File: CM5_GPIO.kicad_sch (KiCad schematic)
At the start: 42 parts, among them J14 JST_BM04B-SRSS-TB, J16 JST_BM04B-SRSS-TB, J19 Conn_1x03_Male, J2 Conn_2x07_Male, J3 Conn_1x03_Male, J7 Micro_SD_Card_Det, J8 Conn_2x20_Male, SW1 Right angle Tact button, SW2 Right angle Tact button, U1 TPD4EUSB30, U16 SN74AHCT1G125DRLR, U17 TCA9538DBR, U18 RT9742GGJ5, U2 TPD4EUSB30, U3 MagJack-A70-112-331N126, U5 74LVC1G07SE-7, U9 SK6812

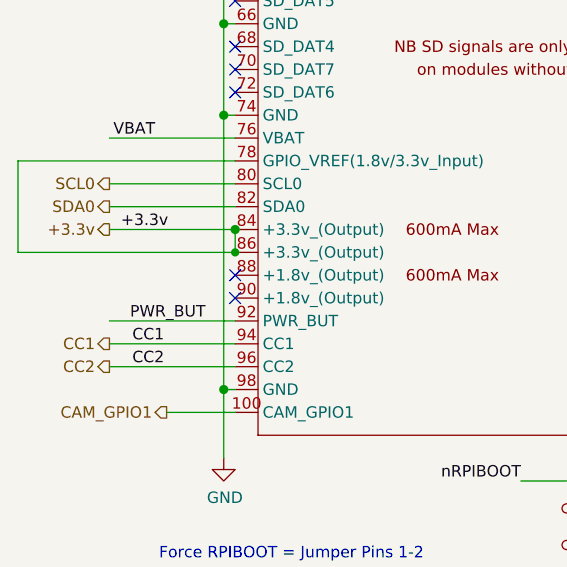
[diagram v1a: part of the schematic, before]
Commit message: USB hub: run the 24 MHz oscillator Y1 from the CM5 1.8 V output
Y1 (ECS-2520MV, 1.6-3.6 V supply) was powered from +3.3 V and drove
U11 XI (pin 30) with a 3.3 V clock. XI is rated 2.45 V absolute maximum
and TI requires a 1.8 V clock source (TUSB4041I datasheet 5.1, 6.3.6).

- Y1 VDD and its decoupling cap C50 move from +3.3v to a new +1V8 net.
- +1V8 comes from the CM5's +1.8 V output pins 88/90 (600 mA total),
  which were unused (no-connect flags removed).
- Y1 tri-state pin 1 gets a no-connect flag: open = output enabled per
  the ECS-2520MV datasheet.

Note: Y1's Value field says ECS-2520MV-240-CN-TR while its MPN/Digikey
fields say -DN-TR (C = +/-25 ppm, D = +/-20 ppm); both meet the hub's
+/-100 ppm. Left as is for the BOM owner to reconcile.

Refs #24 (verify on hardware before closing).

Co-Authored-By: Claude Opus 5.5 <noreply@anthropic.com>
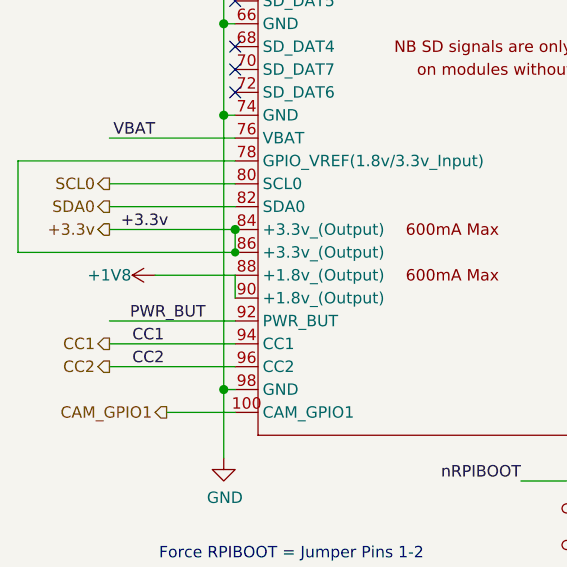
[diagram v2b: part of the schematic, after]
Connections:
- net +1V8: now reaches Module1.88 (+1.8v_(Output))
- net +1V8: now also Module1.90 (+1.8v_(Output))
- no-connect marks 13 -> 11
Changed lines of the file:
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@@
 	)
 	(no_connect
-		(at 39.37 130.81)
-	)
-	(no_connect
 		(at 39.37 107.95)
 	)
@@
 	)
 	(no_connect
-		(at 39.37 133.35)
-	)
-	(no_connect
 		(at 39.37 105.41)
 	)
@@
 	(wire
 		(pts
+			(xy 30.48 130.81) (xy 39.37 130.81)
+		)
+		(stroke
+			(width 0)
+			(type default)
+		)
+	)
+	(wire
+		(pts
 			(xy 149.86 44.45) (xy 152.4 44.45)
 		)
@@
 	(wire
 		(pts
+			(xy 39.37 130.81) (xy 39.37 133.35)
+		)
+		(stroke
+			(width 0)
+			(type default)
+		)
+	)
+	(wire
+		(pts
 			(xy 100.33 24.13) (xy 113.03 24.13)
 		)
@@
 					(unit 1)
 				)
+			)
+		)
+	)
+	(symbol
+		(lib_id "power:+1V8")
+		(at 30.48 130.81 90)
+		(unit 1)
+		(body_style 1)
+		(exclude_from_sim no)
+		(in_bom yes)
+		(on_board yes)
+		(in_pos_files yes)
+		(dnp no)
+		(property "Reference" "#PWR001"
+			(at 34.29 130.81 0)
+			(hide yes)
+			(show_name no)
+			(do_not_autoplace no)
+			(effects
+				(font
+					(size 1.27 1.27)
+				)
+			)
+		)
+		(property "Value" "+1V8"
+			(at 25.4 130.81 90)
+			(show_name no)
+			(do_not_autoplace no)
+			(effects
+				(font
+					(size 1.27 1.27)
+				)
+			)
+		)
+		(property "Footprint" ""
+			(at 30.48 130.81 0)
+			(hide yes)
+			(show_name no)
+			(do_not_autoplace no)
+			(effects
+				(font
+					(size 1.27 1.27)
+				)
+			)
+		)
+		(property "Datasheet" ""
+			(at 30.48 130.81 0)
+			(hide yes)
+			(show_name no)
+			(do_not_autoplace no)
+			(effects
+				(font
+					(size 1.27 1.27)
+				)
+			)
+		)
+		(property "Description" "Power symbol creates a global label with name \"+1V8\""
+			(at 30.48 130.81 0)
+			(hide yes)
+			(show_name no)
+			(do_not_autoplace no)
+			(effects
+				(font
+					(size 1.27 1.27)
+				)
+			)
+		)
+		(pin "1"
+		)
+		(instances
+			(project "libreboard"
+				(path "/e63e39d7-6ac0-4ffd-8aa3-1841a4541b55/00000000-0000-0000-0000-00005cff706a"
+					(reference "#PWR001")
+					(unit 1)
+				)

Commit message: USB hub: software-controlled hub reset from TCA9538 P7
The CM5 can now hard-reset the TUSB4041 hub over I2C, without
power-cycling anything else.

- U17 (TCA9538) P7 drives new net HUB_SW_RESETz into the manual-reset
  input (MR, pin 3) of the hub supervisor U19 (TPS3808G01). MR has an
  internal ~90k pull-up and the TCA9538 has no I/O pull-ups, so at
  power-up (P7 = input) the supervisor alone controls GRSTz as before.
- To reset: write 0 to P7 in the output register (0x01), then clear bit
  7 of the configuration register (0x03) so P7 drives low; after ~1 ms
  set the bit again. U19 holds GRSTz low while MR is low and for its
  20 ms timeout after release, so the hub always gets a valid (>= 3 ms)
  reset pulse regardless of software timing.
- U17 A0/A1 were floating; both now go to GND, fixing the expander at
  0x70 on i2c-0 (ID_SC/ID_SD), the address testscripts already use.
- Root sheet: HUB_SW_RESETz sheet pins on CM5_GPIO (out) and
  CM5_HighSpeed (in), wired like the other inter-sheet signals.

No new parts. PCB needs Update from Schematic and three short traces
(U17.12 to U19.3, U17.1 and U17.2 to GND). Netlist diff: only those
four pins change net. ERC 353 -> 348, only the U17 A0/A1/P7
unconnected warnings go away.

Refs #25.

Co-Authored-By: Claude Opus 5.5 <noreply@anthropic.com>
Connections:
- net GND: now also U17.1 (A0), U17.2 (A1)
- net HUB_SW_RESETz: now reaches U17.12 (P7)
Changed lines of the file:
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@@
 	)
 	(junction
+		(at 54.61 238.76)
+		(diameter 0)
+		(color 0 0 0 0)
+	)
+	(junction
 		(at 21.59 177.8)
 		(diameter 0)
@@
 	(wire
 		(pts
+			(xy 90.17 223.52) (xy 95.25 223.52)
+		)
+		(stroke
+			(width 0)
+			(type default)
+		)
+	)
+	(wire
+		(pts
 			(xy 38.1 95.25) (xy 39.37 95.25)
 		)
@@
 	(wire
 		(pts
+			(xy 54.61 241.3) (xy 54.61 238.76)
+		)
+		(stroke
+			(width 0)
+			(type default)
+		)
+	)
+	(wire
+		(pts
 			(xy 129.54 151.13) (xy 137.16 151.13)
 		)
@@
 	(wire
 		(pts
+			(xy 54.61 238.76) (xy 38.1 238.76)
+		)
+		(stroke
+			(width 0)
+			(type default)
+		)
+	)
+	(wire
+		(pts
 			(xy 165.1 29.21) (xy 166.37 29.21)
 		)
@@
 		)
 	)
+	(hierarchical_label "HUB_SW_RESETz"
+		(shape output)
+		(at 95.25 223.52 0)
+		(effects
+			(font
+				(size 1.27 1.27)
+			)
+			(justify left)
+		)
+	)
 	(hierarchical_label "SCL0"
 		(shape output)
@@
 					(unit 1)
 				)
+			)
+		)
+	)
+	(symbol
+		(lib_id "power:GND")
+		(at 38.1 238.76 0)
+		(unit 1)
+		(body_style 1)
+		(exclude_from_sim no)
+		(in_bom yes)
+		(on_board yes)
+		(in_pos_files yes)
+		(dnp no)
+		(property "Reference" "#PWR142"
+			(at 38.1 245.11 0)
+			(hide yes)
+			(show_name no)
+			(do_not_autoplace no)
+			(effects
+				(font
+					(size 1.27 1.27)
+				)
+			)
+		)
+		(property "Value" "GND"
+			(at 38.1 242.57 0)
+			(show_name no)
+			(do_not_autoplace no)
+			(effects
+				(font
+					(size 1.27 1.27)
+				)
+			)
+		)
+		(property "Footprint" ""
+			(at 38.1 238.76 0)
+			(hide yes)
+			(show_name no)
+			(do_not_autoplace no)
+			(effects
+				(font
+					(size 1.27 1.27)
+				)
+			)
+		)
+		(property "Datasheet" ""
+			(at 38.1 238.76 0)
+			(hide yes)
+			(show_name no)
+			(do_not_autoplace no)
+			(effects
+				(font
+					(size 1.27 1.27)
+				)
+			)
+		)
+		(property "Description" "Power symbol creates a global label with name \"GND\" , ground"
+			(at 38.1 238.76 0)
+			(hide yes)
+			(show_name no)
+			(do_not_autoplace no)
+			(effects
+				(font
+					(size 1.27 1.27)
+				)
+			)
+		)
+		(pin "1"
+		)
+		(instances
+			(project "libreboard"
+				(path "/e63e39d7-6ac0-4ffd-8aa3-1841a4541b55/00000000-0000-0000-0000-00005cff706a"
+					(reference "#PWR142")
+					(unit 1)
+				)

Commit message: Status LED: hold the U16 buffer off by default (R52 pull-up on OE#)
U16 (SN74AHCT1G125) gates the shared SPI0 MOSI line (GPIO10, also
header pin 19) to the SK6812 status LED U9. Its active-low OE# comes
from TCA9538 P0, which is an input at power-up and after any expander
reset, and the TCA9538 has no internal pull-ups. OE# therefore floated:
the buffer could be on from boot and pass a HAT's SPI traffic to the
LED as random colour data.

New R52 10k (0603, ERJ-3EKF1002V) from OE# to +3.3v keeps the buffer
off (LED input held low by R42) until software drives P0 low for an
LED update, so P0 now acts as a proper chip-select for the LED and no
40-pin header pin is used.

Netlist: only R52 added (pin 1 +3.3v, pin 2 on the OE# net with U16.1
and U17.4). ERC unchanged at 348.

Co-Authored-By: Claude Opus 5.5 <noreply@anthropic.com>
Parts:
- added R52: 10kΩ, Resistor_SMD:R_0603_1608Metric, symbol Device:R
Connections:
- net +3.3v: now also R52.1
- net at U16.1 (*OE), U17.4 (P0): now also R52.2
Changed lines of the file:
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@@
 	)
 	(junction
+		(at 101.6 243.84)
+		(diameter 0)
+		(color 0 0 0 0)
+	)
+	(junction
 		(at 245.11 72.39)
 		(diameter 1.016)
@@
 	)
 	(junction
+		(at 101.6 243.84)
+		(diameter 0)
+		(color 0 0 0 0)
+	)
+	(junction
 		(at 38.1 29.21)
 		(diameter 1.016)
@@
 	(wire
 		(pts
-			(xy 90.17 243.84) (xy 113.03 243.84)
-		)
-		(stroke
-			(width 0)
-			(type default)
-		)
-	)
-	(wire
-		(pts
 			(xy 101.6 49.53) (xy 101.6 62.23)
 		)
@@
 	(wire
 		(pts
+			(xy 101.6 236.22) (xy 101.6 233.68)
+		)
+		(stroke
+			(width 0)
+			(type default)
+		)
+	)
+	(wire
+		(pts
 			(xy 44.45 170.18) (xy 58.42 170.18)
 		)
@@
 	(wire
 		(pts
+			(xy 90.17 243.84) (xy 101.6 243.84)
+		)
+		(stroke
+			(width 0)
+			(type default)
+		)
+	)
+	(wire
+		(pts
 			(xy 228.6 36.83) (xy 245.11 36.83)
 		)
@@
 	(wire
 		(pts
+			(xy 101.6 243.84) (xy 113.03 243.84)
+		)
+		(stroke
+			(width 0)
+			(type default)
+		)
+	)
+	(wire
+		(pts
 			(xy 24.13 64.77) (xy 39.37 64.77)
 		)
@@
 		)
 	)
+	(label "+3.3v"
+		(at 101.6 233.68 0)
+		(effects
+			(font
+				(size 1.27 1.27)
+			)
+			(justify left bottom)
+		)
+	)
 	(label "TRD3_N"
 		(at 245.11 54.61 180)
@@
 					(unit 1)
 				)
+			)
+		)
+	)
+	(symbol
+		(lib_id "Device:R")
+		(at 101.6 240.03 0)
+		(unit 1)
+		(body_style 1)
+		(exclude_from_sim no)
+		(in_bom yes)
+		(on_board yes)
+		(in_pos_files yes)
+		(dnp no)
+		(property "Reference" "R52"
+			(at 105.41 238.76 0)
+			(show_name no)
+			(do_not_autoplace no)
+			(effects
+				(font
+					(size 1.27 1.27)
+				)
+			)
+		)
+		(property "Value" "10kΩ"
+			(at 105.41 241.3 0)
+			(show_name no)
+			(do_not_autoplace no)
+			(effects
+				(font
+					(size 1.27 1.27)
+				)
+			)
+		)
+		(property "Footprint" "Resistor_SMD:R_0603_1608Metric"
+			(at 101.6 240.03 0)
+			(hide yes)
+			(show_name no)
+			(do_not_autoplace no)
+			(effects
+				(font
+					(size 1.27 1.27)
+				)
+			)
+		)
+		(property "Datasheet" ""
+			(at 101.6 240.03 0)
+			(hide yes)
+			(show_name no)
+			(do_not_autoplace no)
+			(effects
+				(font
+					(size 1.27 1.27)
+				)
+			)
+		)
+		(property "Description" "Resistor"
+			(at 101.6 240.03 0)
+			(hide yes)
+			(show_name no)
+			(do_not_autoplace no)
+			(effects
+				(font
+					(size 1.27 1.27)
+				)
+			)
+		)
+		(property "Dist. P/N" "P10.0KHTR-ND"
+			(at 101.6 240.03 0)
+			(hide yes)
+			(show_name no)
+			(do_not_autoplace no)
+			(effects
+				(font
+					(size 1.27 1.27)
+				)
+			)
+		)
+		(property "Distributor" "Digikey"
+			(at 101.6 240.03 0)
+			(hide yes)
+			(show_name no)
+			(do_not_autoplace no)
+			(effects
+				(font
+					(size 1.27 1.27)
+				)
+			)
+		)
+		(property "Manf. P/N" "ERJ-3EKF1002V"
+			(at 101.6 240.03 0)
+			(hide yes)
+			(show_name no)
+			(do_not_autoplace no)
+			(effects
+				(font
+					(size 1.27 1.27)
+				)
+			)
+		)
+		(property "Manufacturer" "Panasonic"
+			(at 101.6 240.03 0)
+			(hide yes)
+			(show_name no)
+			(do_not_autoplace no)
+			(effects
+				(font
+					(size 1.27 1.27)
+				)
+			)
+		)
+		(property "Part Description" "Resistor, 10kΩ, ±1%, 0.1W, SMD 0603 (1608m)"
+			(at 101.6 240.03 0)
+			(hide yes)
+			(show_name no)
+			(do_not_autoplace no)
+			(effects
+				(font
+					(size 1.27 1.27)
+				)
+			)
+		)
+		(pin "1"
+		)
+		(pin "2"
+		)
+		(instances
+			(project "libreboard"
+				(path "/e63e39d7-6ac0-4ffd-8aa3-1841a4541b55/00000000-0000-0000-0000-00005cff706a"
+					(reference "R52")
+					(unit 1)
+				)

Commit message: Status LED: R52 OE# pull-up in 0402
The 0603 footprint was hard to fit next to U16. R52 now uses the same
0402 10k (Panasonic ERJ-U02F1002X) as R4, R29, R30 and the other 10k
pull-ups, so it adds no BOM line. No connectivity change.

Co-Authored-By: Claude Opus 5.5 <noreply@anthropic.com>
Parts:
- R52: footprint Resistor_SMD:R_0603_1608Metric -> Resistor_SMD:R_0402_1005Metric; Dist. P/N P10.0KHTR-ND -> 10-ERJ-U02F1002XTR-ND; Manf. P/N ERJ-3EKF1002V -> ERJ-U02F1002X; Part Description Resistor, 10kΩ, ±1%, 0.1W, SMD 0603 (1608m) -> Resistor, 10kΩ, ±1%, 0.1W, SMD 0402 (1005m)
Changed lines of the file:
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@@
 			)
 		)
-		(property "Footprint" "Resistor_SMD:R_0603_1608Metric"
+		(property "Footprint" "Resistor_SMD:R_0402_1005Metric"
 			(at 101.6 240.03 0)
 			(hide yes)
@@
 			)
 		)
-		(property "Dist. P/N" "P10.0KHTR-ND"
+		(property "Dist. P/N" "10-ERJ-U02F1002XTR-ND"
 			(at 101.6 240.03 0)
 			(hide yes)
@@
 			)
 		)
-		(property "Manf. P/N" "ERJ-3EKF1002V"
+		(property "Manf. P/N" "ERJ-U02F1002X"
 			(at 101.6 240.03 0)
 			(hide yes)
@@
 			)
 		)
-		(property "Part Description" "Resistor, 10kΩ, ±1%, 0.1W, SMD 0603 (1608m)"
+		(property "Part Description" "Resistor, 10kΩ, ±1%, 0.1W, SMD 0402 (1005m)"
 			(at 101.6 240.03 0)
 			(hide yes)

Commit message: HUB_3V3 also feeds the status LEDs, R52 and the TCA9538
The hub-side 3.3 V copper on the PCB also runs on to D1/D2/U5, R52
and U17/R4, so those move onto the hub's always-on rail too:

- U5 + D1 (red power LED): the CM5's LED_nPWR is meant to light the
  red LED while the board is powered but shut down, and the CM5's
  3.3 V output is off exactly then (CM5 datasheet, pins 84/86), so the
  standby LED never worked. On HUB_3V3 it can.
- D2 (green ACT LED): LED_nACT is 5 V tolerant open drain, so no
  back-powering into a shut-down CM5.
- R52 (U16 OE# pull-up): U16 runs from +5v; on HUB_3V3 the LED gate
  stays shut while the CM5's 3.3 V is still down at boot.
- U17 TCA9538 + R4: same rail as the hub reset (U19 MR) and LED gate
  it drives; I2C pins are open drain, no back-powering. The expander
  now keeps its register state across CM5 shutdowns (resets on +5v).

HUB_3V3 becomes a top-level net (/HUB_3V3): hierarchical labels on
the CM5_HighSpeed (U20 output) and CM5_GPIO sheets, sheet pins and a
labelled wire on the root sheet. 15 nodes on /HUB_3V3; /+3.3v keeps
the camera, J15 Rp, fan controller, I2C pull-ups, SD switch, header,
Qwiic and Ethernet LEDs. ERC unchanged at 346.

Co-Authored-By: Claude Opus 5.5 <noreply@anthropic.com>
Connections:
- net +3.3v: no longer D1.2 (A), D2.2 (A), R4.2, R52.1, U17.16 (VCC), U5.5 (VCC)
- new net HUB_3V3: D1.2 (A), D2.2 (A), R4.2, R52.1, U17.16 (VCC), U5.5 (VCC)
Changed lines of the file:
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@@
-		)
-	)
-	(label "+3.3v"
-		(at 101.6 233.68 0)
-		(effects
-			(font
-				(size 1.27 1.27)
-			)
-			(justify left bottom)
 		)
 	)
@@
 		)
 	)
-	(label "+3.3v"
-		(at 116.84 19.05 180)
+	(label "HUB_3V3"
+		(at 172.72 115.57 180)
 		(effects
 			(font
@@
 		)
 	)
-	(label "+3.3v"
-		(at 35.56 251.46 0)
-		(effects
-			(font
-				(size 1.27 1.27)
-			)
-			(justify left bottom)
-		)
-	)
 	(label "TRD3_P"
 		(at 245.11 49.53 180)
@@
 		)
 	)
+	(label "HUB_3V3"
+		(at 35.56 251.46 0)
+		(effects
+			(font
+				(size 1.27 1.27)
+			)
+			(justify left bottom)
+		)
+	)
 	(label "SD_CLK"
 		(at 110.49 92.71 180)
@@
 		)
 	)
-	(label "+3.3v"
-		(at 161.29 132.08 180)
-		(effects
-			(font
-				(size 1.27 1.27)
-			)
-			(justify right bottom)
-		)
-	)
 	(label "nRPIBOOT"
 		(at 104.14 138.43 0)
@@
 		)
 	)
+	(label "HUB_3V3"
+		(at 116.84 19.05 180)
+		(effects
+			(font
+				(size 1.27 1.27)
+			)
+			(justify right bottom)
+		)
+	)
 	(label "ID_SC"
 		(at 109.22 64.77 180)
@@
 		)
 	)
-	(label "+3.3v"
-		(at 172.72 115.57 180)
-		(effects
-			(font
-				(size 1.27 1.27)
-			)
-			(justify right bottom)
-		)
-	)
 	(label "GPIO13"
 		(at 148.59 64.77 180)
@@
 	(label "GPIO15"
 		(at 137.16 115.57 180)
+		(effects
+			(font
+				(size 1.27 1.27)
+			)
+			(justify right bottom)
+		)
+	)
+	(label "HUB_3V3"
+		(at 161.29 132.08 180)
 		(effects
 			(font
@@
 		)
 	)
+	(hierarchical_label "HUB_3V3"
+		(shape input)
+		(at 101.6 233.68 0)
+		(effects
+			(font
+				(size 1.27 1.27)
+			)
+			(justify left)
+		)
+	)

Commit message: BOM: LCSC codes for JLCPCB assembly, DigiKey numbers verified
Sourcing pass for a rev3 build at JLCPCB (SMT + through-hole), keeping
the DigiKey BOM usable. Report and per-part data in bom/rev3-sourcing.*.

- New hidden "LCSC" field on 189 parts (88 of 93 part numbers).
  Passives use JLC Basic/Preferred equivalents where value, size,
  tolerance, voltage and dielectric match or improve (0402 resistors at
  62.5 mW: worst-case dissipation on this board < 5 mW); ICs and
  connectors use the exact part. Exact codes are stored even where JLC
  has no stock (U4/U14, U3, U16, U17, BT1) - see the report.
- DigiKey: every existing number checked against its MPN (reel numbers
  kept). Filled: J7 (was Farnell 2358234), C60 (AVX new PN
  KGM05ACG1H6R8CH), C61, C66-C68, Q1/Q2, U20, U21. C73: wrong number
  (490-1494-2-ND is GRM188R71H102KA01D) cleared - to fill by hand.
- C72: Murata GRM188R71C104KA01D is obsolete -> Yageo CC0603KRX7R9BB104
  (0.1 uF 50 V X7R 0603).
- Fixes: L2/L3 manufacturer Coilcraft -> Bourns; U9 distributor typo
  LSCS -> LCSC; C27-C29 DigiKey number without " - Cut Tape" suffix.

Not yet stored: Y1, J2, J8, SW1/SW2 candidates need review; M1 is a
screw. Connectivity, values and footprints unchanged; ERC unchanged
at 342.

Co-Authored-By: Claude Opus 5.5 <noreply@anthropic.com>
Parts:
- BT1: LCSC (none) -> C7219081
- C1, C70: LCSC (none) -> C1525
- C5: LCSC (none) -> C15850
- C71: LCSC (none) -> C15525
- D1: LCSC (none) -> C125114
- D2: LCSC (none) -> C125113
- J14, J16: LCSC (none) -> C160390
- J19, J3: LCSC (none) -> C505002
- J7: Dist. P/N 2358234 -> WM11190TR-ND; Distributor Farnell -> Digikey; LCSC (none) -> C428492
- R1, R10: LCSC (none) -> C11702
- R2, R3, R9: LCSC (none) -> C25117
- R4, R52: LCSC (none) -> C25744
- R42: LCSC (none) -> C25741
- U1, U2: LCSC (none) -> C90627
- U16: LCSC (none) -> C507216
- U17: LCSC (none) -> C2652331
- U18: LCSC (none) -> C250547
- U3: LCSC (none) -> C37415176
- U5: LCSC (none) -> C67531
- U9: Distributor LSCS -> LCSC
